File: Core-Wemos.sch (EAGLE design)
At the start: 50 parts, among them J2 CONNECTOR-GROVE-4P-2.0-347013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, J3 IO4

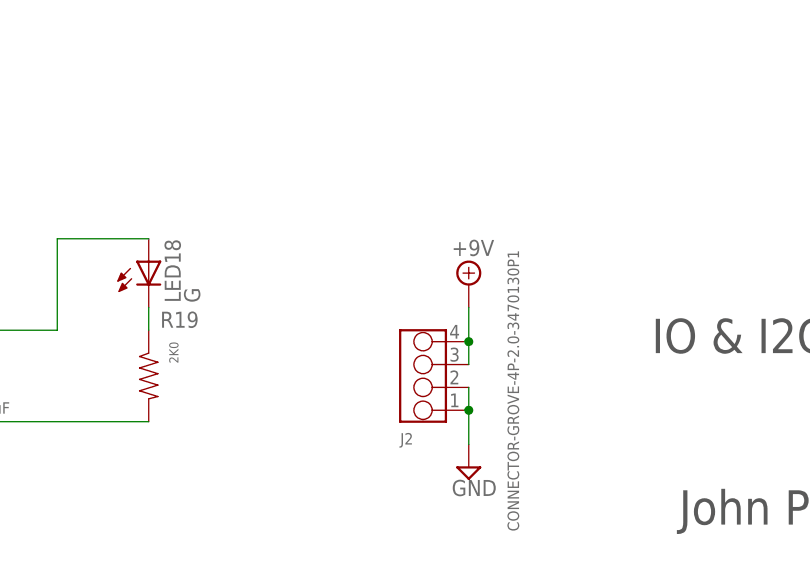
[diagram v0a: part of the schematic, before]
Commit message: Moved OLED, added 1x4 0.100 VIN
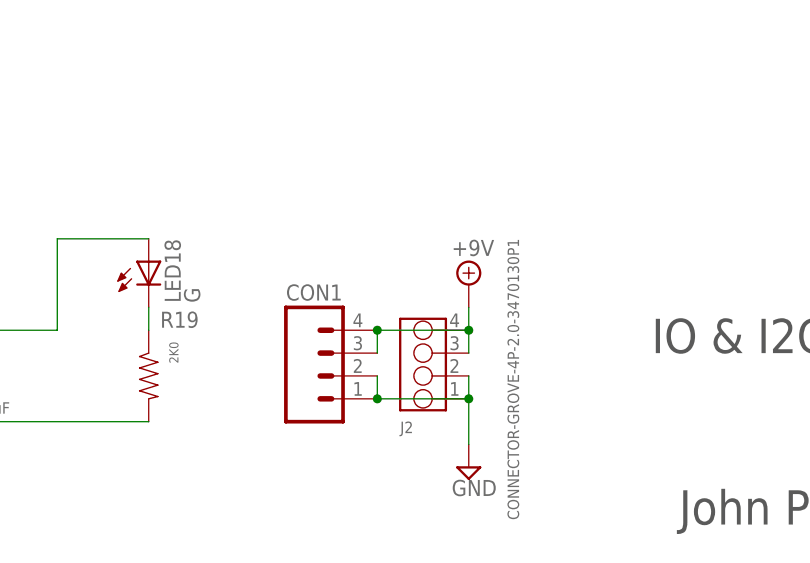
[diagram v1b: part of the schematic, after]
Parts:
- added CON1: (no value), SPCoast:CONNECTOR-M04LOCK
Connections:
- net +9V: now also CON1.3, CON1.4
- net GND: now also CON1.1, CON1.2
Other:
- moved on the sheet: J2

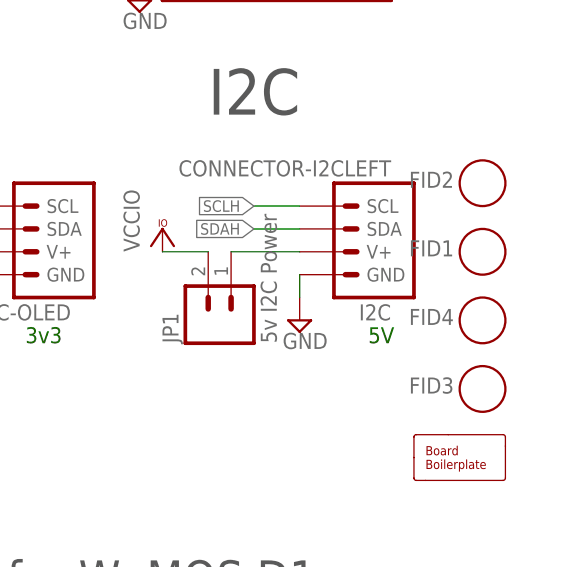
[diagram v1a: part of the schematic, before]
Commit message: Renamed/Moved FIDs
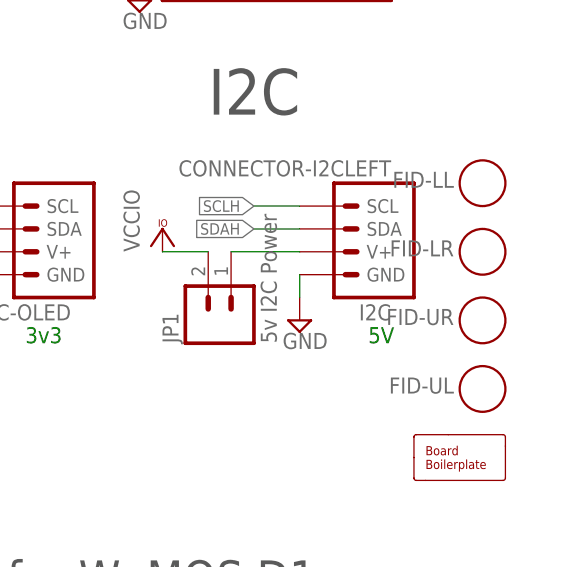
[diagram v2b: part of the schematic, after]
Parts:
- renumbered FID1 to FID-LR, FID2 to FID-LL, FID3 to FID-UL, FID4 to FID-UR
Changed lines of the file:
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@@
 <part name="V2" library="supply2" deviceset="GND" device=""/>
 <part name="VCC2" library="supply1" deviceset="VCCIO" device=""/>
-<part name="FID3" library="SPCoast" deviceset="FIDUCIAL" device=""/>
-<part name="FID1" library="SPCoast" deviceset="FIDUCIAL" device=""/>
-<part name="FID2" library="SPCoast" deviceset="FIDUCIAL" device=""/>
-<part name="FID4" library="SPCoast" deviceset="FIDUCIAL" device=""/>
+<part name="FID-UL" library="SPCoast" deviceset="FIDUCIAL" device=""/>
+<part name="FID-LR" library="SPCoast" deviceset="FIDUCIAL" device=""/>
+<part name="FID-LL" library="SPCoast" deviceset="FIDUCIAL" device=""/>
+<part name="FID-UR" library="SPCoast" deviceset="FIDUCIAL" device=""/>
 <part name="I2C-OLED" library="SPCoast" deviceset="CONNECTOR-I2C" device="NOOUTLINE"/>
 <part name="V4" library="supply2" deviceset="GND" device=""/>
@@
 <instance part="V2" gate="GND" x="60.96" y="55.88"/>
 <instance part="VCC2" gate="G$1" x="53.34" y="63.5"/>
-<instance part="FID3" gate="FID1" x="243.84" y="48.26"/>
-<instance part="FID1" gate="FID1" x="243.84" y="63.5"/>
-<instance part="FID2" gate="FID1" x="243.84" y="71.12"/>
-<instance part="FID4" gate="FID1" x="243.84" y="55.88"/>
+<instance part="FID-UL" gate="FID1" x="243.84" y="48.26"/>
+<instance part="FID-LR" gate="FID1" x="243.84" y="63.5"/>
+<instance part="FID-LL" gate="FID1" x="243.84" y="71.12"/>
+<instance part="FID-UR" gate="FID1" x="243.84" y="55.88"/>
 <instance part="I2C-OLED" gate="I2C" x="195.58" y="63.5" rot="R180"/>
 <instance part="V4" gate="GND" x="185.42" y="58.42"/>

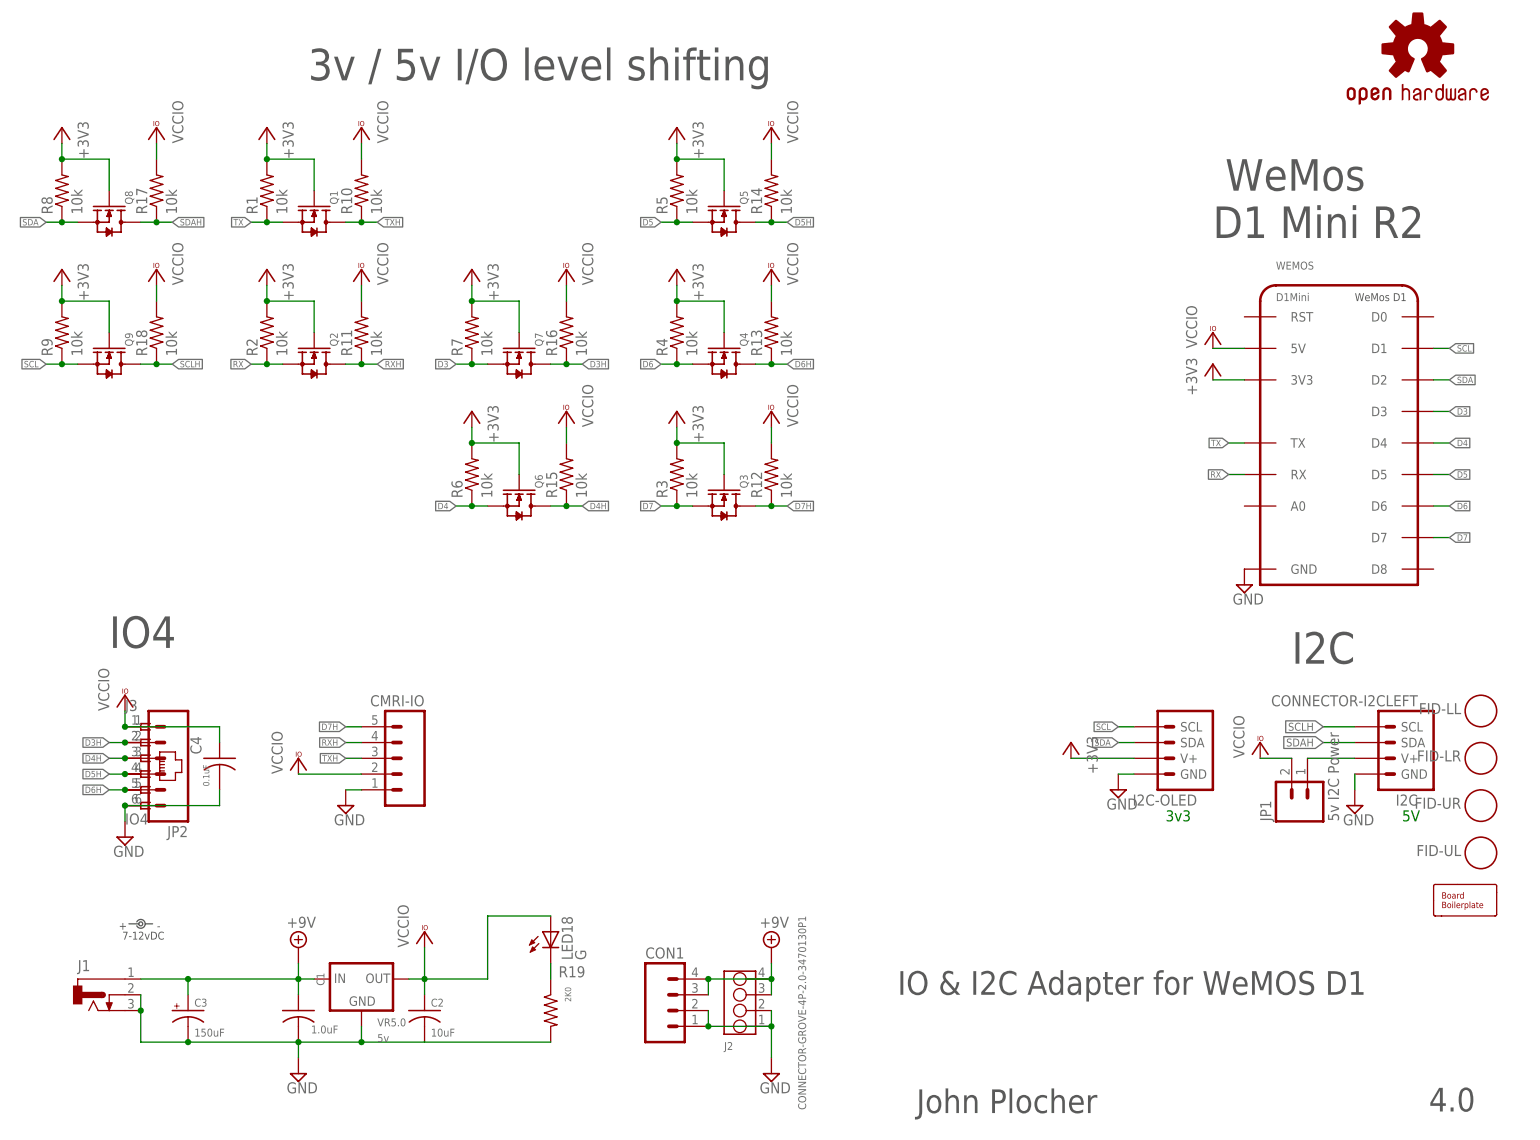
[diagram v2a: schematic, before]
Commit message: added missing component values
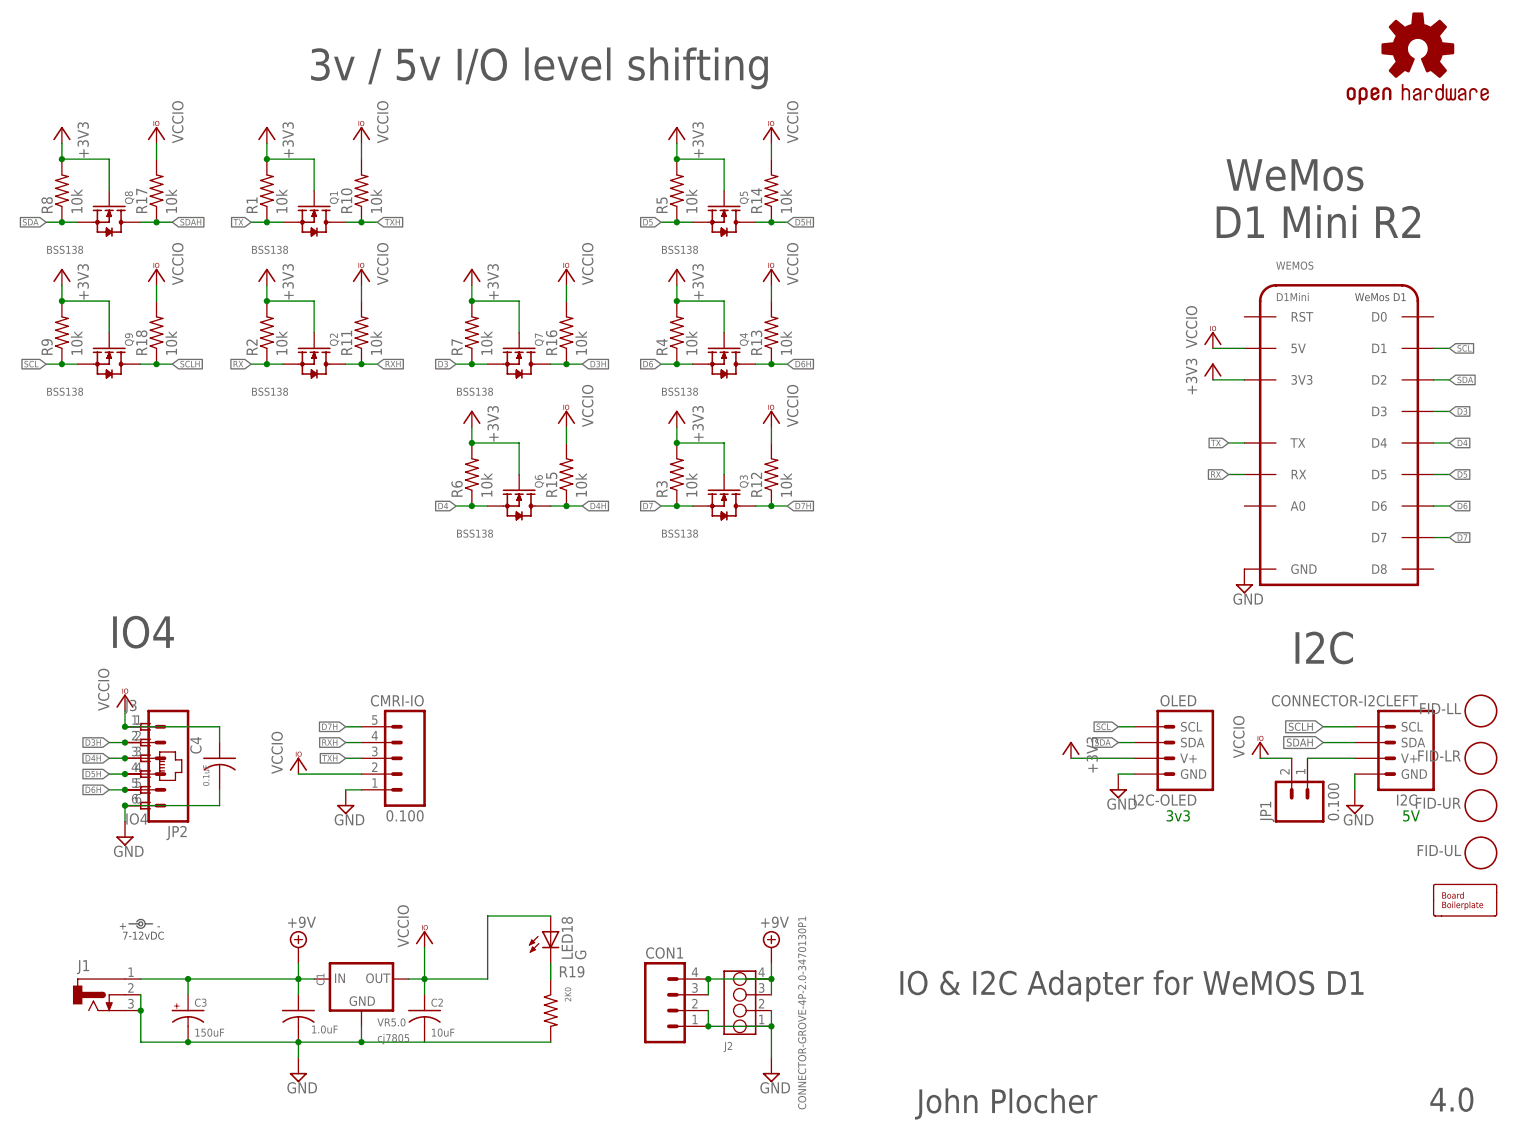
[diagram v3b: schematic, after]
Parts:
- CMRI-IO: value (none) -> 0.100
- I2C-OLED: value (none) -> OLED
- JP1: value 5v I2C Power -> 0.100
- Q1, Q2, Q3, Q4, Q5, Q6, Q7, Q8, Q9: value (none) -> BSS138
- VR5.0: value 5v -> cj7805

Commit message: updated part names and values
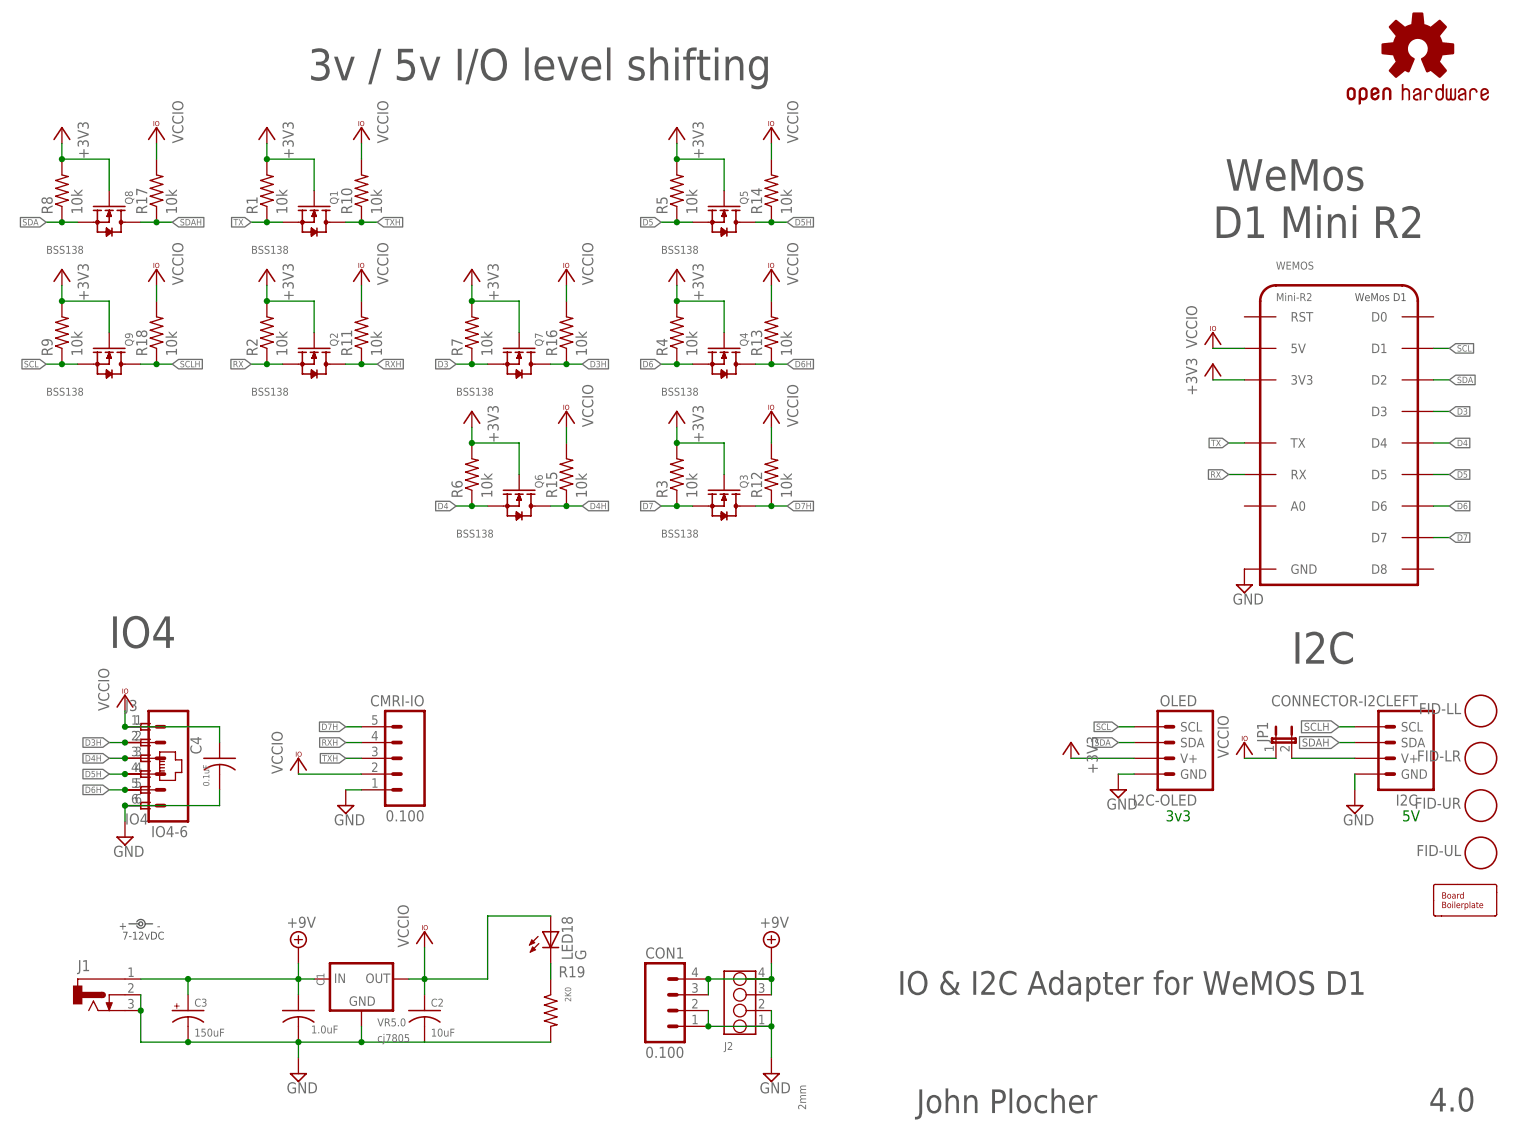
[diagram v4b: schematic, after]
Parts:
- removed JP2: (no value), SparkFun-Connectors:M06LOCK
- added IO4-6: (no value), SPCoast:CONNECTOR-M06LOCK
- CON1: value (none) -> 0.100
- J2: value CONNECTOR-GROVE-4P-2.0-3470130P1 -> 2mm
- JP1: value 0.100 -> (none); device SparkFun-Connectors:M02LOCK -> SPCoast:JUMPER-2PTH_LOCK
- WEMOS: value D1Mini -> Mini-R2
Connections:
- net D3H: now also IO4-6.2; no longer JP2.2
- net D4H: now also IO4-6.3; no longer JP2.3
- net D5H: now also IO4-6.4; no longer JP2.4
- net D6H: now also IO4-6.5; no longer JP2.5
- net GND: now also IO4-6.6; no longer JP2.6
- net N$44: now also JP1.2; no longer JP1.1
- net VCCIO: now also IO4-6.1, JP1.1; no longer JP1.2, JP2.1

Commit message: FIDs
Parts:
- removed FID-LL, FID-UR: FIDUCIAL, SPCoast:FIDUCIAL
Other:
- moved on the sheet: FID-LR, FID-UL
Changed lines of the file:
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@@
 <part name="FID-UL" library="SPCoast" deviceset="FIDUCIAL" device=""/>
 <part name="FID-LR" library="SPCoast" deviceset="FIDUCIAL" device=""/>
-<part name="FID-LL" library="SPCoast" deviceset="FIDUCIAL" device=""/>
-<part name="FID-UR" library="SPCoast" deviceset="FIDUCIAL" device=""/>
 <part name="I2C-OLED" library="SPCoast" deviceset="CONNECTOR-I2C" device="NOOUTLINE" value="OLED"/>
 <part name="V4" library="supply2" deviceset="GND" device=""/>
@@
 <instance part="V2" gate="GND" x="60.96" y="55.88"/>
 <instance part="VCC2" gate="G$1" x="53.34" y="63.5"/>
-<instance part="FID-UL" gate="FID1" x="243.84" y="48.26"/>
-<instance part="FID-LR" gate="FID1" x="243.84" y="63.5"/>
-<instance part="FID-LL" gate="FID1" x="243.84" y="71.12"/>
-<instance part="FID-UR" gate="FID1" x="243.84" y="55.88"/>
+<instance part="FID-UL" gate="FID1" x="243.84" y="50.8"/>
+<instance part="FID-LR" gate="FID1" x="243.84" y="45.72"/>
 <instance part="I2C-OLED" gate="I2C" x="195.58" y="63.5" rot="R180"/>
 <instance part="V4" gate="GND" x="185.42" y="58.42"/>
